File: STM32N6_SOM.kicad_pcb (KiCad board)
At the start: 8 copper layers, 88 parts, among them J1 DF40C-100DP-0.4V_51_, J2 DF40C-100DP-0.4V_51_, U1 STM32N657X0H3Q, U2 TPSM82822ASILR, U3 TPS22914BYFPR, U5 512Mbit

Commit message: All components placed, pwr decoupling routing in progress
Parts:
- removed C10, C9: 100nF, Capacitor_SMD:C_0201_0603Metric
- removed C17: 1µF, Capacitor_SMD:C_0201_0603Metric
- removed C63, C64: 4.7µF, Capacitor_SMD:C_0402_1005Metric
- removed R37: 0R, Capacitor_SMD:C_0402_1005Metric
- removed R60: 10k, Capacitor_SMD:C_0402_1005Metric
- removed U4: ~, PLib:tfbga24 (6_8mm2)
- added C15: 100nF, Capacitor_SMD:C_0201_0603Metric, F.Cu at (153.8, 64.5)
- added C16: 100nF, Capacitor_SMD:C_0201_0603Metric, F.Cu at (153.8, 66.3)
- added C65: 4.7µF, Capacitor_SMD:C_0402_1005Metric, F.Cu at (143.6, 64.6)
- added C67: 4.7µF, Capacitor_SMD:C_0402_1005Metric, F.Cu at (143.6, 66.6)
- added L3: 1µH, Capacitor_SMD:C_0805_2012Metric, F.Cu at (144.4, 79.9)
- added R1: 470k, Resistor_SMD:R_0402_1005Metric, F.Cu at (117.8, 62.7)
- added R2: 2, Resistor_SMD:R_0402_1005Metric, F.Cu at (117.8, 64.7)
- added R3: 200k, Resistor_SMD:R_0402_1005Metric, F.Cu at (117.8, 66.7)
- added R38: 0R, Capacitor_SMD:C_0402_1005Metric, F.Cu at (143.6, 68.6)
- added R4: 200, Resistor_SMD:R_0402_1005Metric, F.Cu at (127.2, 62.7)
- added R5: 100k, Resistor_SMD:R_0402_1005Metric, F.Cu at (117.8, 68.6)
- added R6: 200, Resistor_SMD:R_0402_1005Metric, F.Cu at (127.2, 64.7)
- added R61: 10k, Capacitor_SMD:C_0402_1005Metric, F.Cu at (143.6, 70.5)
- added R62: 10k, Capacitor_SMD:C_0402_1005Metric, F.Cu at (143.6, 72.5)
- added R7: 200, Resistor_SMD:R_0402_1005Metric, F.Cu at (127.2, 66.7)
- added U7: ~, PLib:tfbga24 (6_8mm2), F.Cu at (130.9, 77.5)
- added Y2: Crystal, PLib:C1987116, F.Cu at (109.8, 77.7)
- added Y3: Crystal_GND24, PLib:C1985871, F.Cu at (125.2, 71.3)
- C23, C27, C70: moved to F.Cu
- FB1: footprint Capacitor_SMD:C_0603_1608Metric -> Inductor_SMD:L_0201_0603Metric
- U2: value TPSM82822ASILR -> TPSM82823ASILR
- U3: value TPS22914BYFPR -> TPS22915BYFPR
- moved C14 30.1 mm to (118.0, 79.2)
- moved C72 29.7 mm to (124.3, 85.6), turned to 0 degrees
- moved C75 28.7 mm to (124.3, 84.8), turned to 0 degrees
- moved C71 28.0 mm to (122.4, 84.5), turned to -90 degrees
- moved C76 27.8 mm to (123.5, 84.0), turned to 0 degrees
- moved C73 27.7 mm to (122.4, 86.8), turned to -90 degrees
- moved C74 27.4 mm to (122.7, 85.7), turned to 0 degrees
- moved C79 26.5 mm to (119.6, 79.2), turned to 0 degrees
- moved C13 25.5 mm to (115.2, 86.9), turned to 90 degrees
- moved C38 24.4 mm to (121.6, 84.4), turned to -90 degrees
- moved C39 24.4 mm to (121.6, 86.0), turned to -90 degrees
- moved C77 24.1 mm to (119.2, 80.4), turned to -90 degrees
- moved C78 23.8 mm to (118.4, 80.4), turned to -90 degrees
- moved C37 22.4 mm to (118.4, 85.2), turned to 90 degrees
- moved C24 21.6 mm to (122.0, 80.8)
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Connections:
- J1 pad 10: unconnected-(J1-Pad10) -> VDD3V3
- J1 pad 11: unconnected-(J1-Pad11) -> VDD3V3
- J1 pad 12: unconnected-(J1-Pad12) -> VDD3V3
- J1 pad 13: unconnected-(J1-Pad13) -> GND
- J1 pad 14: unconnected-(J1-Pad14) -> GND
- J1 pad 7: GND -> VDD3V3
- J1 pad 8: GND -> VDD3V3
- J1 pad 9: unconnected-(J1-Pad9) -> VDD3V3
- R53 pad 1: Net-(U5-RESET#) -> /NRST
- R54 pad 2: Net-(U5-RESET#) -> /NRST
- U5 pad A4: Net-(U5-RESET#) -> /NRST
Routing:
- net GND: track 0.00 -> 13.2 mm, vias 5 -> 16
- net Net-(U1A-V08CAP): track 0.00 -> 2.37 mm
- net Net-(U1A-VDDA18PMU): track 0.00 -> 2.34 mm, vias 1 -> 0
- net VDD3V3: track 0.00 -> 2.30 mm, vias 0 -> 6
- net VDD1V8: track 0.00 -> 1.16 mm, vias 1 -> 10
- net VDDCORE: vias 2 -> 10
- net VDDA1V8_AON: vias 1 -> 0
- net VDD3V3_EXT: vias 1 -> 5

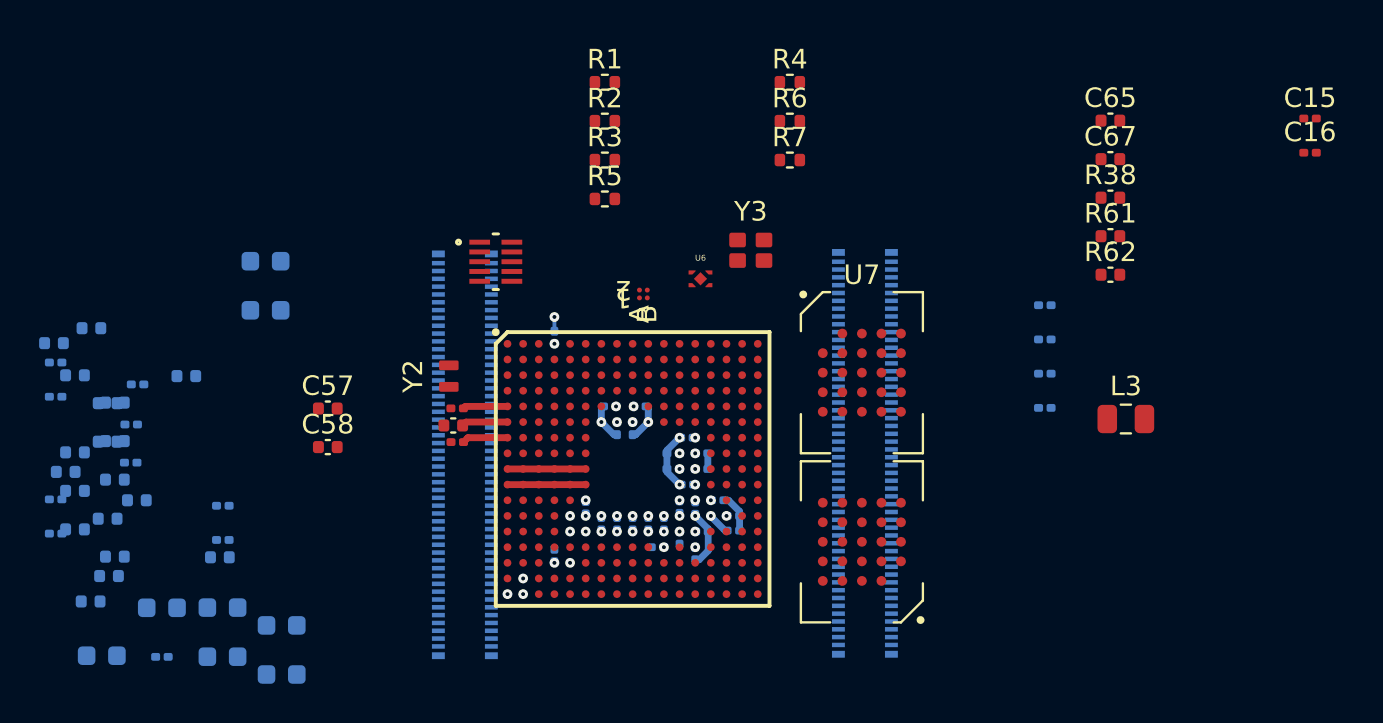
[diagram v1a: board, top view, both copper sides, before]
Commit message: Power decoupling done, will work on pwr supplies next then connector routing
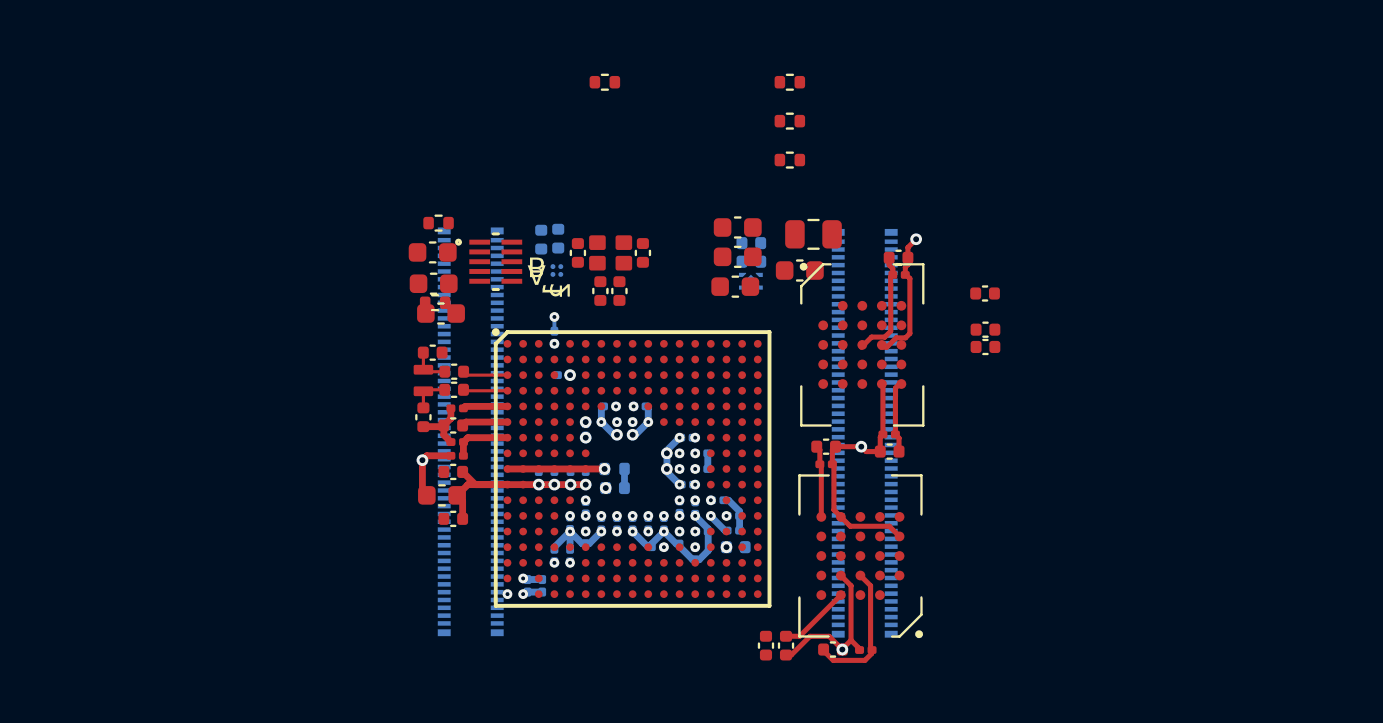
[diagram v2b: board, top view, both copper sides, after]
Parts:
- removed R54: 10k, Capacitor_SMD:C_0402_1005Metric
- C19, C29, C30, C31, C32, C52, C53, C55, C6, C66, C68, C7, C8, C84, C85, C86, C87, FB1, L1, R53, R55, R56, R57, R58, R59: moved to F.Cu
- C57, C58, R2, U3, U6: moved to B.Cu
- moved C8 43.4 mm to (131.1, 91.7), turned to 0 degrees
- moved C7 39.7 mm to (129.1, 82.2)
- moved R53 36.8 mm to (127.0, 91.5), turned to -90 degrees
- moved C84 36.4 mm to (129.1, 81.3)
- moved C85 36.4 mm to (129.4, 91.7)
- moved C32 33.6 mm to (127.8, 72.3), turned to 0 degrees
- moved R59 32.7 mm to (126.0, 91.5), turned to -90 degrees
- moved R57 29.9 mm to (118.5, 73.3), turned to -90 degrees
- moved C31 29.0 mm to (124.5, 73.1)
- moved R55 28.9 mm to (117.5, 73.3), turned to 90 degrees
- moved C86 28.3 mm to (116.4, 71.4), turned to 90 degrees
- moved C56 28.1 mm to (114.5, 70.7), turned to 90 degrees
- moved C66 28.1 mm to (119.7, 71.4), turned to -90 degrees
- moved C54 27.9 mm to (115.4, 70.7), turned to 90 degrees
- moved C28 27.7 mm to (118.3, 83.4)
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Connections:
- L1 pad 1: VDD1V8 -> Net-(C19-Pad1)
- L1 pad 2: Net-(C19-Pad1) -> VDD1V8
- L3 pad 1: Net-(L3-Pad1) -> VDDCORE
- L3 pad 2: VDDCORE -> Net-(L3-Pad2)
- R2 pad 2: Net-(L3-Pad1) -> Net-(L3-Pad2)
- U1 pad J1: Net-(L3-Pad1) -> Net-(L3-Pad2)
- U1 pad J2: Net-(L3-Pad1) -> Net-(L3-Pad2)
- U1 pad J3: Net-(L3-Pad1) -> Net-(L3-Pad2)
- U1 pad J4: Net-(L3-Pad1) -> Net-(L3-Pad2)
- U1 pad J5: Net-(L3-Pad1) -> Net-(L3-Pad2)
- U1 pad J6: Net-(L3-Pad1) -> Net-(L3-Pad2)
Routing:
- net GND: track 13.2 -> 46.5 mm, vias 16 -> 23
- net VDD1V8: track 1.16 -> 34.2 mm, vias 10 -> 14
- net Net-(C19-Pad1): track 4.00 -> 10.7 mm, vias 0 -> 4
- net Net-(L3-Pad2): track 0.00 -> 4.97 mm, vias 0 -> 1
- net Net-(L3-Pad1): track 4.00 -> 0.00 mm
- net /NRST: track 0.00 -> 3.68 mm
- net /PC15-OSC32_OUT: track 0.00 -> 2.32 mm
- net /PC14-OSC32_IN: track 0.00 -> 2.27 mm
- net Net-(C68-Pad1): track 0.00 -> 2.01 mm
- net Net-(C87-Pad1): track 0.00 -> 1.97 mm
- net Net-(C28-Pad1): track 0.00 -> 0.98 mm
- net Net-(U1A-VDDA18PMU): track 2.34 -> 3.05 mm
- net VDDA1V8_AON: vias 0 -> 1
- net /PN6: vias 0 -> 1

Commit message: Power routing should be done, to be checked, next memory and mezzanine
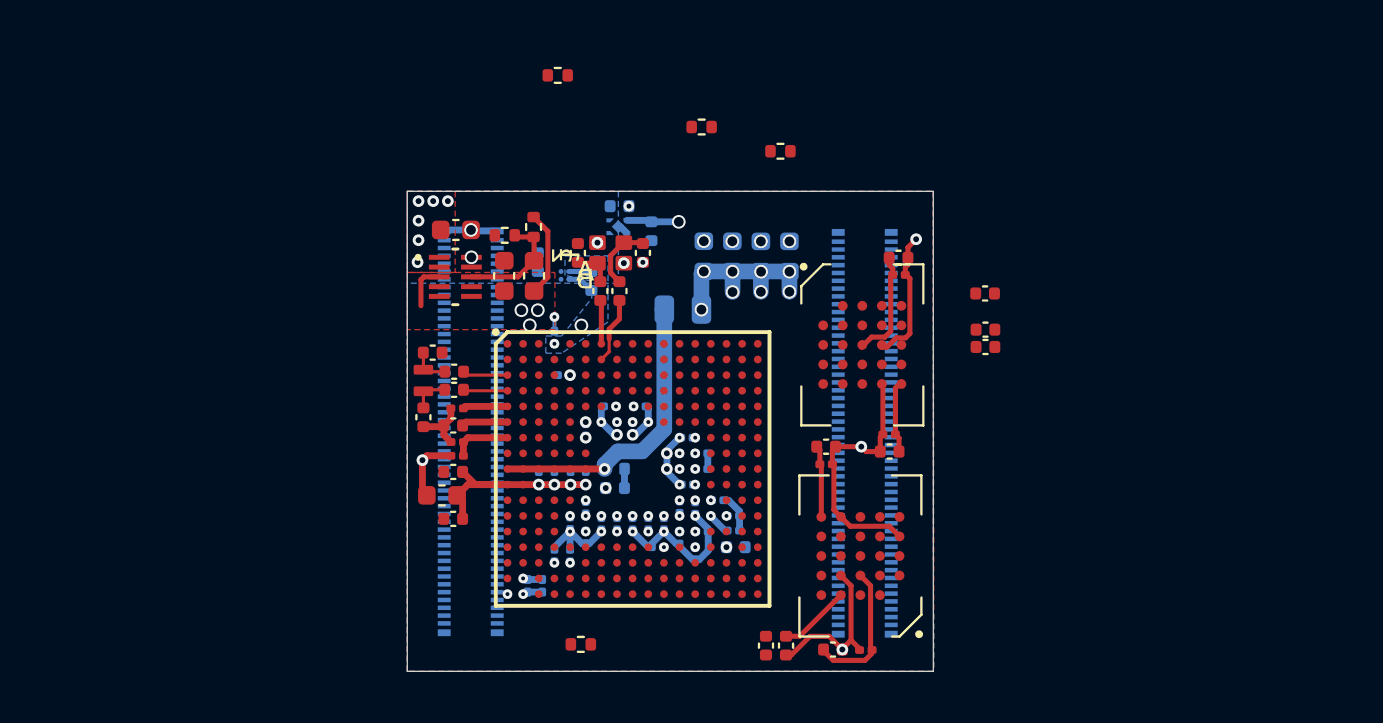
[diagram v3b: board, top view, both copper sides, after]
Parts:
- C29, C30, C31, C32, L3: moved to B.Cu
- moved R4 30.7 mm to (116.5, 91.4), turned to 180 degrees
- moved L3 7.71 mm to (121.8, 74.3)
- moved U6 7.33 mm to (118.5, 70.1)
- moved C57 7.00 mm to (118.5, 69.0), turned to 0 degrees
- moved C58 5.35 mm to (120.2, 70.3), turned to -90 degrees
- moved C55 5.15 mm to (114.2, 72.6), turned to 90 degrees
- moved R5 4.96 mm to (112.7, 70.5), turned to 180 degrees
- moved R3 4.86 mm to (114.1, 70.1), turned to -90 degrees
- moved R7 4.82 mm to (122.7, 65.0)
- moved C53 3.76 mm to (112.6, 72.6), turned to 90 degrees
- moved C56 3.33 mm to (117.1, 72.8), turned to -90 degrees
- moved R1 2.44 mm to (115.4, 62.3)
- moved C29 2.28 mm to (122.8, 71.6), turned to 90 degrees
- moved U2 2.21 mm to (110.1, 72.6)
- moved C31 2.02 mm to (125.8, 71.6), turned to 90 degrees
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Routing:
- net Net-(L3-Pad2): track 4.97 -> 15.2 mm
- net VDDCORE: track 0.00 -> 9.51 mm, vias 10 -> 18
- net Net-(U2-FB): track 0.00 -> 5.80 mm
- net GND: track 46.5 -> 51.2 mm, vias 23 -> 33
- net VDD1V8: track 34.2 -> 38.6 mm, vias 14 -> 17
- net Net-(C66-Pad1): track 0.00 -> 3.46 mm
- net /PH1-OSC_OUT: track 0.00 -> 3.40 mm
- net VDDA1V8_AON: track 0.00 -> 2.69 mm, vias 1 -> 2
- net /PWR/PWR_ON: track 0.00 -> 2.33 mm
- net /PH0-OSC_IN: track 0.00 -> 2.24 mm
- net Net-(C86-Pad1): track 0.00 -> 2.03 mm
- net VDD3V3_EXT: track 0.00 -> 1.15 mm, vias 5 -> 6
- net VDD3V3: vias 6 -> 12
- added copper zone on B.Cu, net GND
- added copper zone on F.Cu, net GND
- added copper zone on F.Cu, net VDD1V8
- added copper zone on B.Cu, net VDD3V3
- added copper zone on F.Cu, net VDD3V3
- added copper zone on B.Cu, net VDD3V3_EXT
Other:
- board outline added: 26.9 x 24.5 mm
